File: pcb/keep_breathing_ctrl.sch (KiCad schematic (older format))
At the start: 4 parts

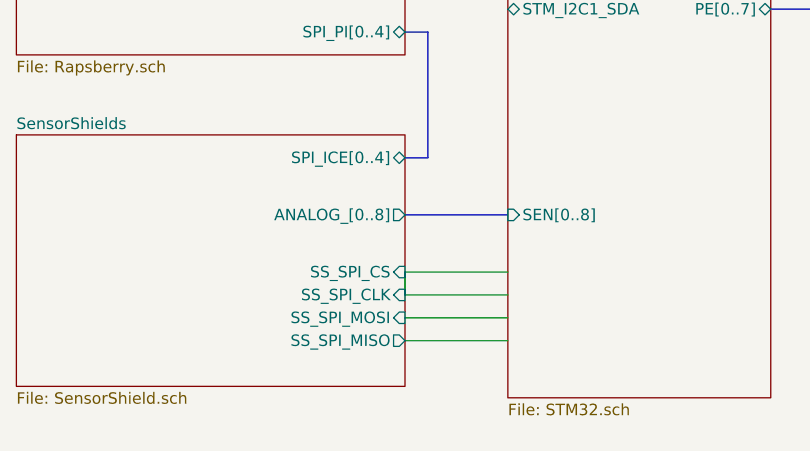
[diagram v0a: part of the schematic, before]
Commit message: SS_SPI_CLK shortcut fixed
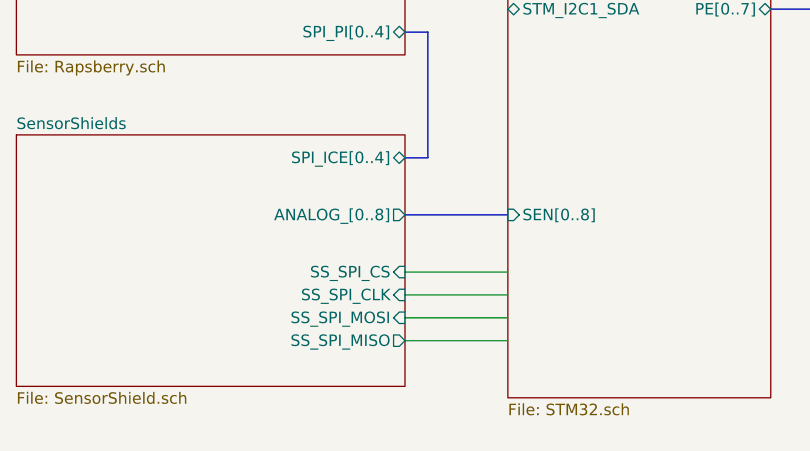
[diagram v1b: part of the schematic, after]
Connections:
- wire segments 20 -> 19
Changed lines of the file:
@@
 EESchema Schematic File Version 4
-LIBS:keep_breathing_ctrl-cache
 EELAYER 30 0
 EELAYER END
@@
 	5800 4450 6250 4450
 Wire Wire Line
-	5800 4700 5800 4800
-Wire Wire Line
 	5800 4800 6250 4800

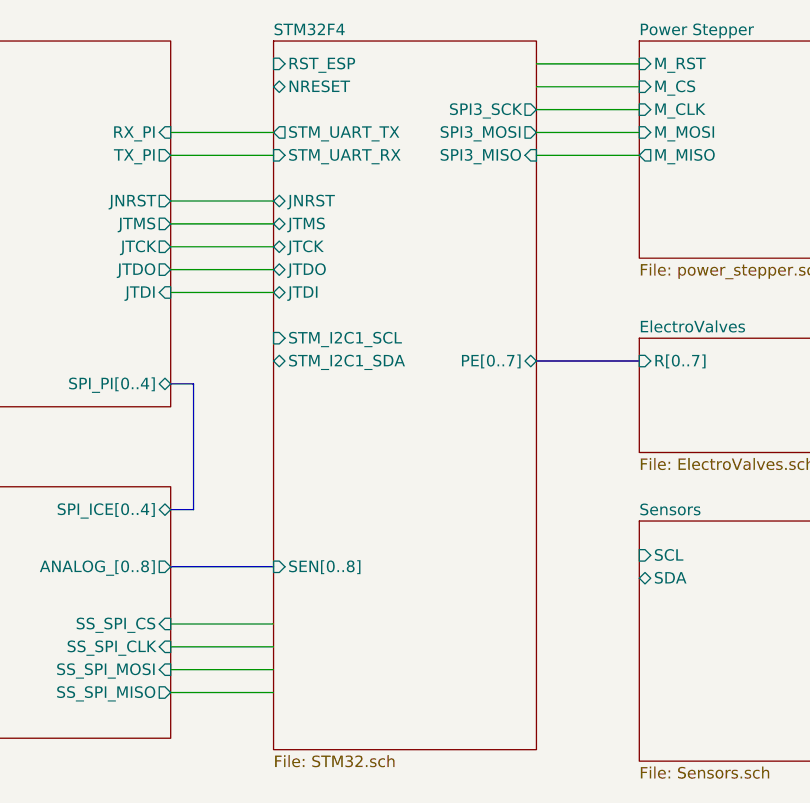
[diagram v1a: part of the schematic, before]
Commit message: connecting SPI signals from STM32
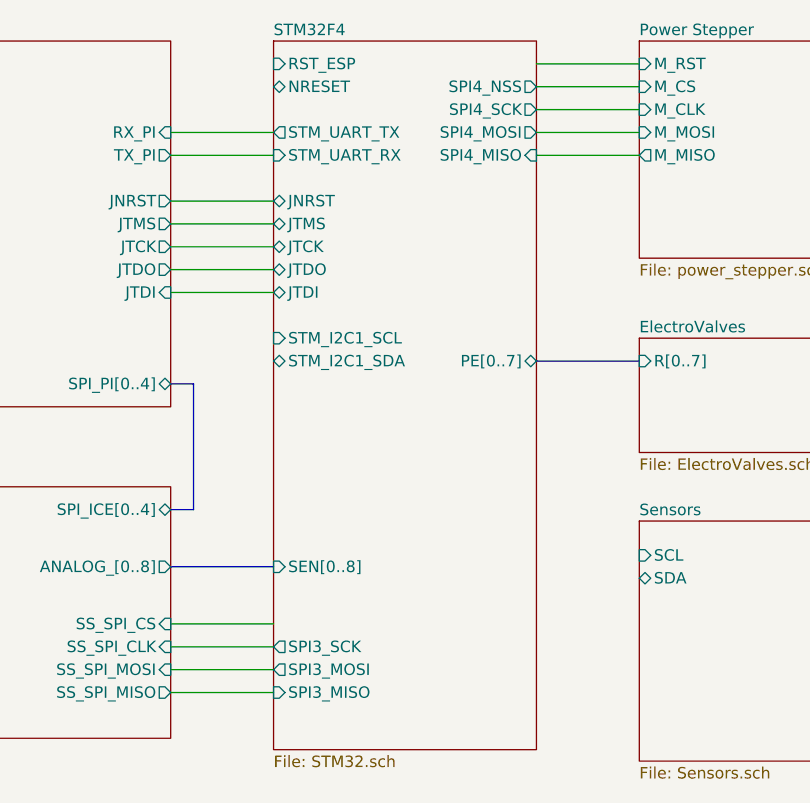
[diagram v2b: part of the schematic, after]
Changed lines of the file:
@@
 F11 "STM_UART_TX" O L 6250 2550 50
 F12 "STM_UART_RX" I L 6250 2650 50
-F13 "SPI3_MOSI" O R 7400 2550 50
-F14 "SPI3_MISO" I R 7400 2650 50
+F13 "SPI3_MOSI" O L 6250 4900 50
+F14 "SPI3_MISO" I L 6250 5000 50
 F15 "PE[0..7]" B R 7400 3550 50
 F16 "SEN[0..8]" I L 6250 4450 50
-F17 "SPI3_SCK" O R 7400 2450 50
+F17 "SPI3_SCK" O L 6250 4800 50
+F18 "SPI4_SCK" O R 7400 2450 50
+F19 "SPI4_MISO" I R 7400 2650 50
+F20 "SPI4_MOSI" O R 7400 2550 50
+F21 "SPI4_NSS" O R 7400 2350 50
 $EndSheet
 $Sheet

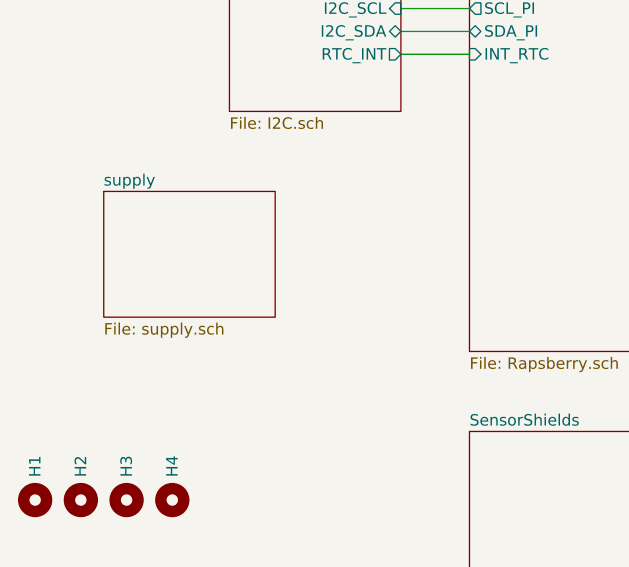
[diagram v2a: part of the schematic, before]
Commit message: protection circuit added
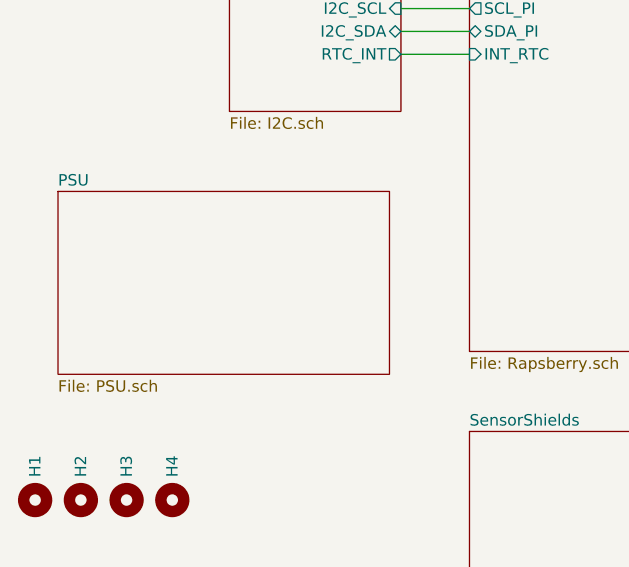
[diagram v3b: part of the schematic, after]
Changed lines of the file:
@@
 EESchema Schematic File Version 4
+LIBS:keep_breathing_ctrl-cache
 EELAYER 30 0
 EELAYER END
@@
 	0    -1   -1   0
 $EndComp
-$Sheet
-S 2500 3050 750  550
-U 5E8E60A3
-F0 "supply" 50
-F1 "supply.sch" 50
-$EndSheet
 Wire Wire Line
 	5800 2550 6250 2550
@@
 Wire Wire Line
 	7850 2350 7400 2350
+$Sheet
+S 2300 3050 1450 800
+U 5EA61A2E
+F0 "PSU" 50
+F1 "PSU.sch" 50
+$EndSheet
 $EndSCHEMATC

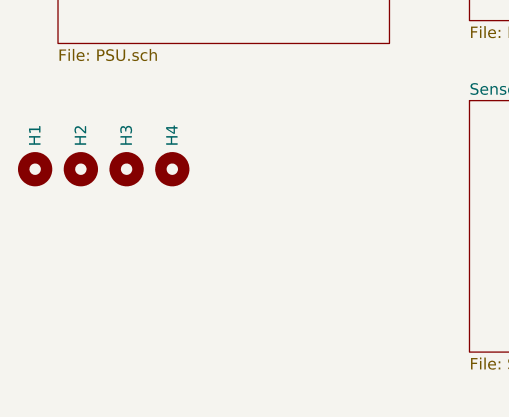
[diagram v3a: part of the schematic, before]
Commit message: mounting holes
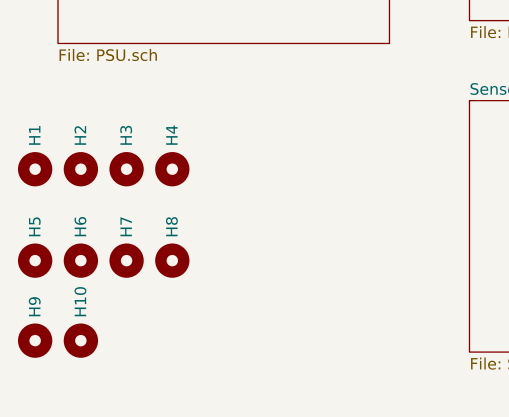
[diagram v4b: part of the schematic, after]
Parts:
- added H10, H5, H6, H7, H8, H9: MountingHole, MountingHole:MountingHole_2.7mm_M2.5, symbol Mechanical:MountingHole
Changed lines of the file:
@@
 F1 "PSU.sch" 50
 $EndSheet
+$Comp
+L Mechanical:MountingHole H5
+U 1 1 5EA83E11
+P 2200 4800
+F 0 "H5" H 2300 4800 50  0000 L CNN
+F 1 "MountingHole" H 2300 4755 50  0001 L CNN
+F 2 "MountingHole:MountingHole_2.7mm_M2.5" H 2200 4800 50  0001 C CNN
+F 3 "~" H 2200 4800 50  0001 C CNN
+	1    2200 4800
+	0    -1   -1   0
+$EndComp
+$Comp
+L Mechanical:MountingHole H6
+U 1 1 5EA83E1B
+P 2400 4800
+F 0 "H6" H 2500 4800 50  0000 L CNN
+F 1 "MountingHole" H 2500 4755 50  0001 L CNN
+F 2 "MountingHole:MountingHole_2.7mm_M2.5" H 2400 4800 50  0001 C CNN
+F 3 "~" H 2400 4800 50  0001 C CNN
+	1    2400 4800
+	0    -1   -1   0
+$EndComp
+$Comp
+L Mechanical:MountingHole H7
+U 1 1 5EA83E25
+P 2600 4800
+F 0 "H7" H 2700 4800 50  0000 L CNN
+F 1 "MountingHole" H 2700 4755 50  0001 L CNN
+F 2 "MountingHole:MountingHole_2.7mm_M2.5" H 2600 4800 50  0001 C CNN
+F 3 "~" H 2600 4800 50  0001 C CNN
+	1    2600 4800
+	0    -1   -1   0
+$EndComp
+$Comp
+L Mechanical:MountingHole H8
+U 1 1 5EA83E2F
+P 2800 4800
+F 0 "H8" H 2900 4800 50  0000 L CNN
+F 1 "MountingHole" H 2900 4755 50  0001 L CNN
+F 2 "MountingHole:MountingHole_2.7mm_M2.5" H 2800 4800 50  0001 C CNN
+F 3 "~" H 2800 4800 50  0001 C CNN
+	1    2800 4800
+	0    -1   -1   0
+$EndComp
+$Comp
+L Mechanical:MountingHole H9
+U 1 1 5EA88269
+P 2200 5150
+F 0 "H9" H 2300 5150 50  0000 L CNN
+F 1 "MountingHole" H 2300 5105 50  0001 L CNN
+F 2 "MountingHole:MountingHole_2.7mm_M2.5" H 2200 5150 50  0001 C CNN
+F 3 "~" H 2200 5150 50  0001 C CNN
+	1    2200 5150
+	0    -1   -1   0
+$EndComp
+$Comp
+L Mechanical:MountingHole H10
+U 1 1 5EA88273
+P 2400 5150
+F 0 "H10" H 2500 5150 50  0000 L CNN
+F 1 "MountingHole" H 2500 5105 50  0001 L CNN
+F 2 "MountingHole:MountingHole_2.7mm_M2.5" H 2400 5150 50  0001 C CNN
+F 3 "~" H 2400 5150 50  0001 C CNN
+	1    2400 5150
+	0    -1   -1   0
+$EndComp
 $EndSCHEMATC

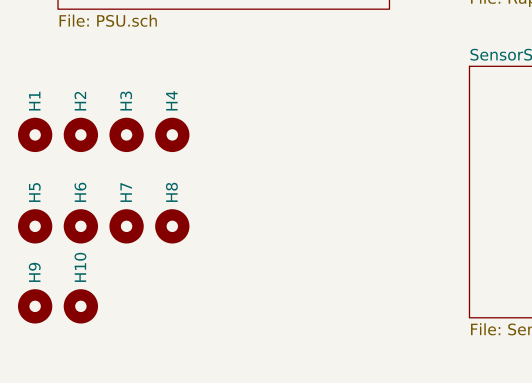
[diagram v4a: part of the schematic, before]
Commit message: adding  mounting holes
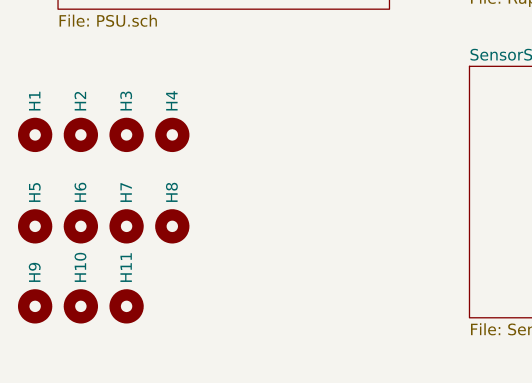
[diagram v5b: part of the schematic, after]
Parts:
- added H11: MountingHole, MountingHole:MountingHole_2.7mm_M2.5, symbol Mechanical:MountingHole
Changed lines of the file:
@@
 EESchema Schematic File Version 4
-LIBS:keep_breathing_ctrl-cache
 EELAYER 30 0
 EELAYER END
@@
 	0    -1   -1   0
 $EndComp
+$Comp
+L Mechanical:MountingHole H11
+U 1 1 5EA7A600
+P 2600 5150
+F 0 "H11" H 2700 5150 50  0000 L CNN
+F 1 "MountingHole" H 2700 5105 50  0001 L CNN
+F 2 "MountingHole:MountingHole_2.7mm_M2.5" H 2600 5150 50  0001 C CNN
+F 3 "~" H 2600 5150 50  0001 C CNN
+	1    2600 5150
+	0    -1   -1   0
+$EndComp

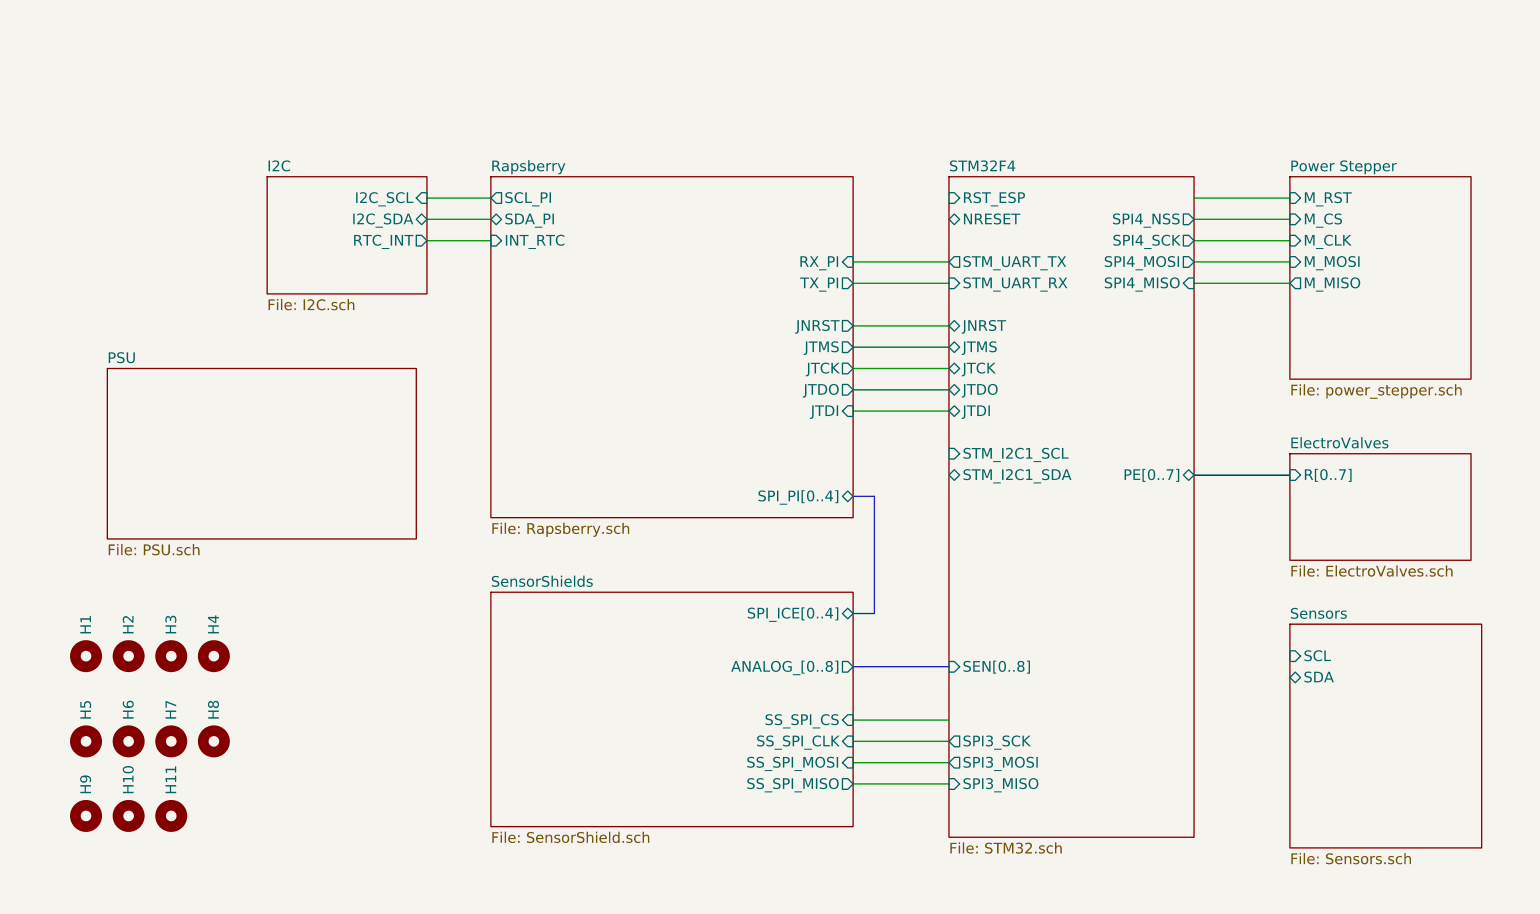
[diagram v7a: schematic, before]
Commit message: fixing missed footprints
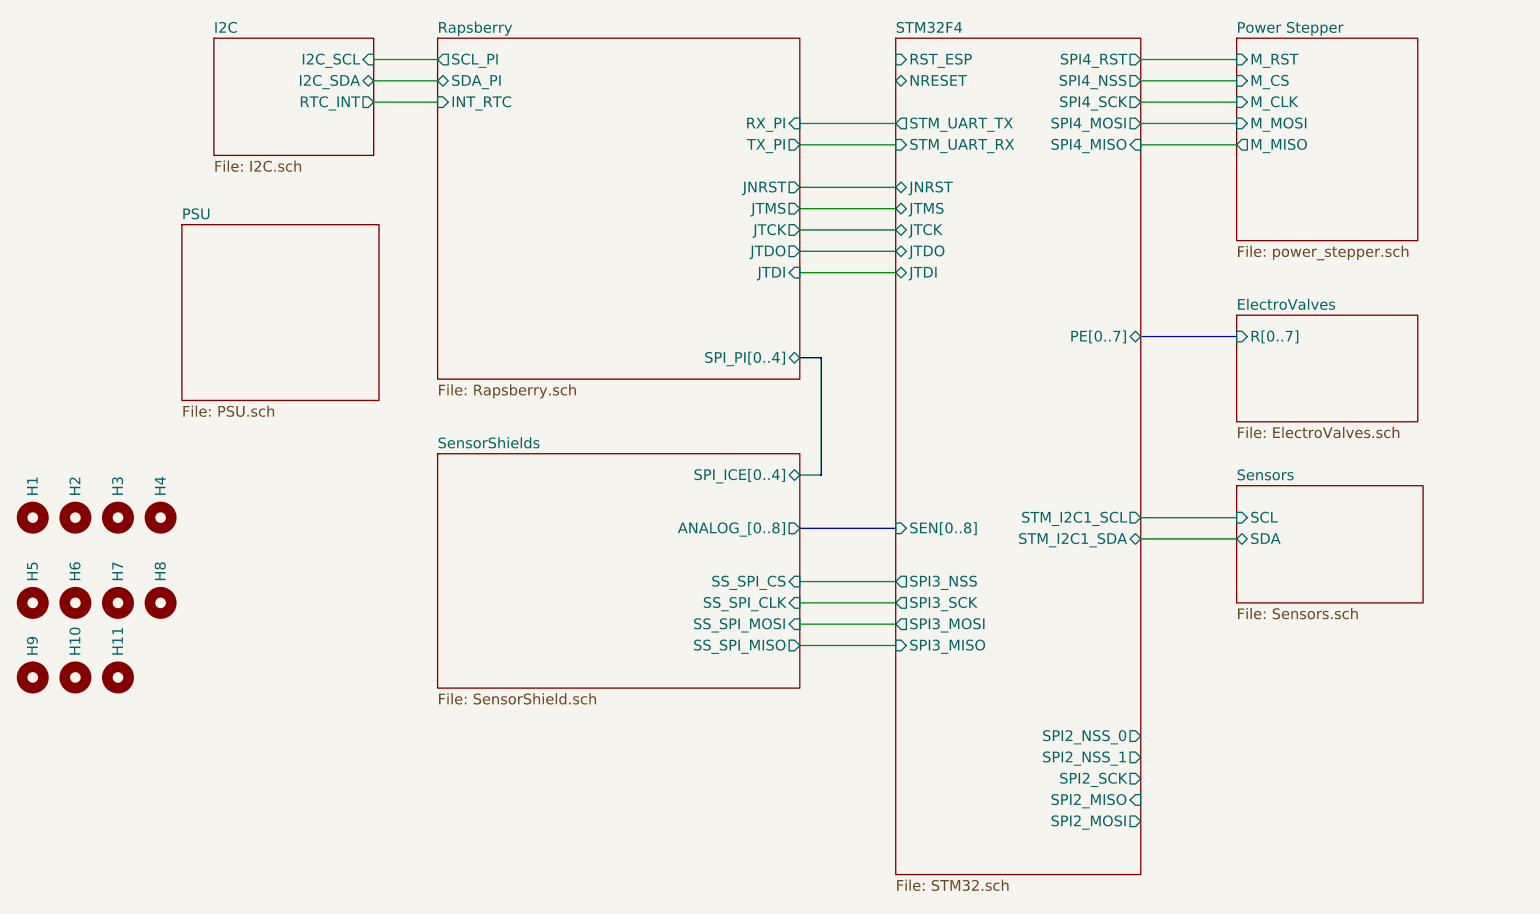
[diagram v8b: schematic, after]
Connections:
- wire segments 19 -> 21
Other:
- moved on the sheet: H1, H10, H11, H2, H3, H4, H5, H6, H7, H8, H9
